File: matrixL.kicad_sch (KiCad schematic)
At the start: 66 parts, among them SW1 SW_Push, SW10 SW_Push, SW11 SW_Push, SW12 SW_Push, SW13 SW_Push, SW14 SW_Push, SW15 SW_Push, SW16 SW_Push, SW17 SW_Push, SW18 SW_Push, SW19 SW_Push, SW2 SW_Push, SW20 SW_Push, SW21 SW_Push, SW22 SW_Push, SW23 SW_Push, SW24 SW_Push, SW25 SW_Push, SW26 SW_Push, SW27 SW_Push, SW28 SW_Push, SW29 SW_Push, SW3 SW_Push, SW30 SW_Push, SW31 SW_Push, SW32 SW_Push, SW33 SW_Push, SW4 SW_Push, SW5 SW_Push, SW6 SW_Push, SW7 SW_Push, SW8 SW_Push, SW9 SW_Push

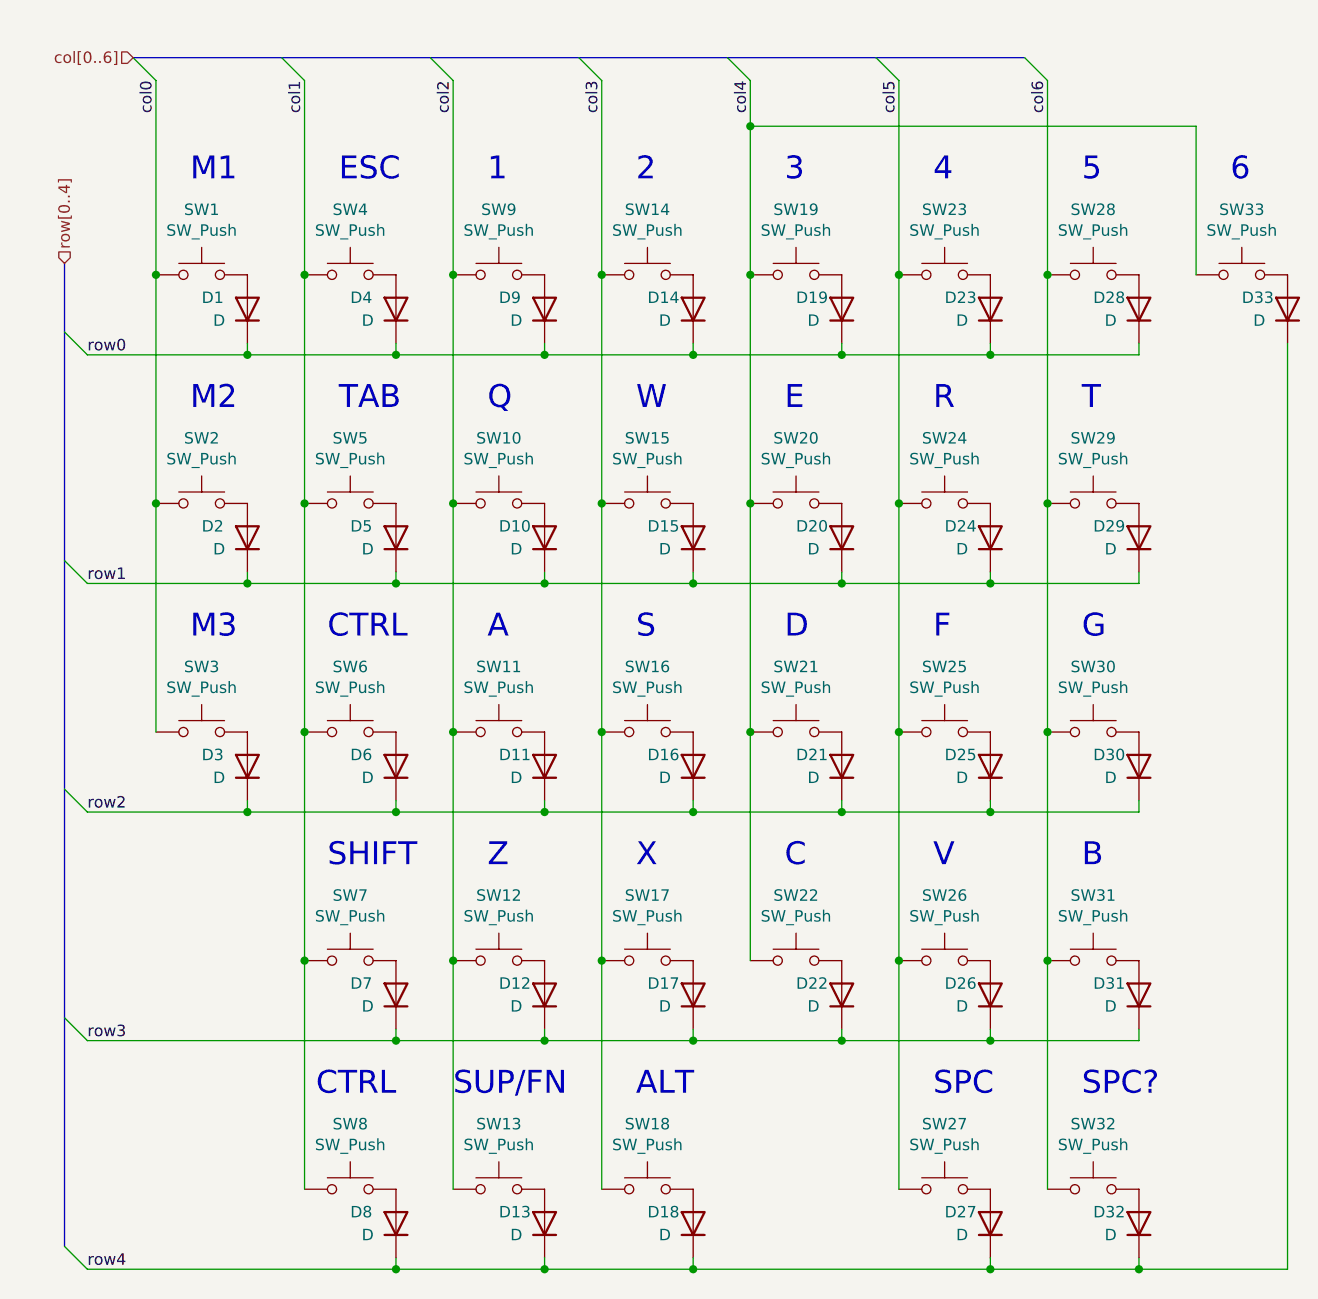
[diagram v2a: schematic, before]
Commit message: Add second micro back in, and added some footprints
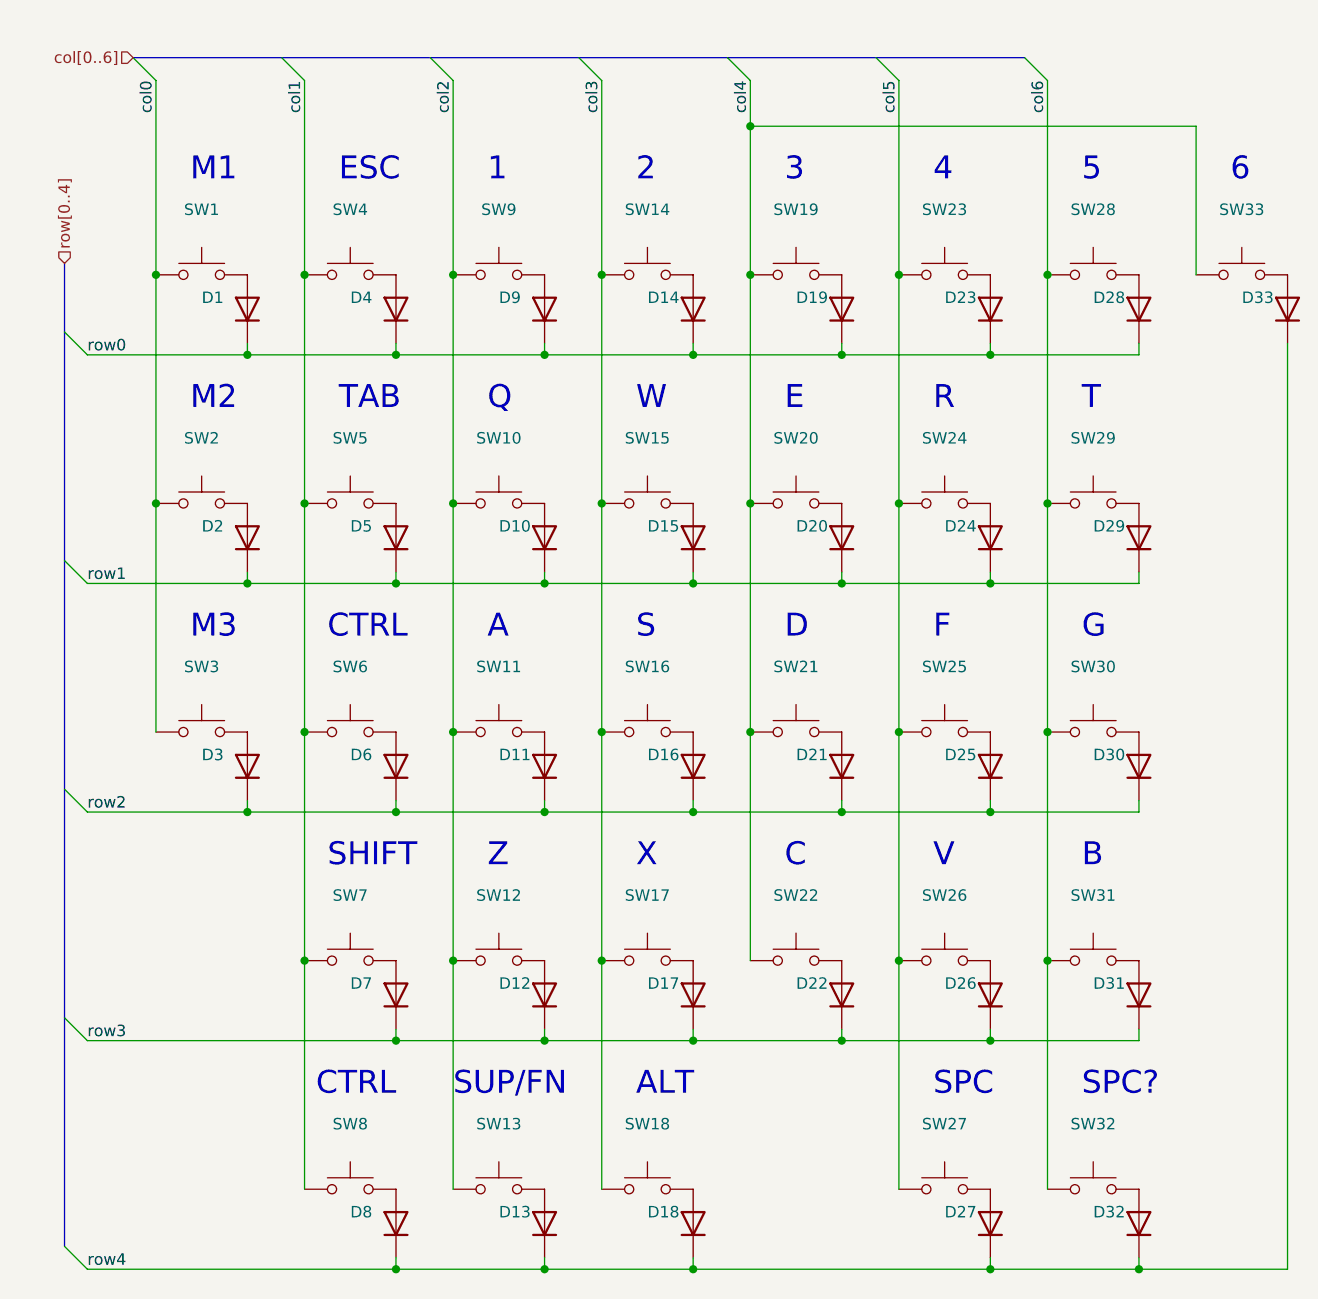
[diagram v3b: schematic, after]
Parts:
- D1, D10, D11, D12, D13, D14, D15, D16, D17, D18, D19, D2, D20, D21, D22, D23, D24, D25, D26, D27, D28, D29, D3, D30, D31, D32, D33, D4, D5, D6, D7, D8, D9: value D -> ~
- SW1, SW10, SW11, SW12, SW13, SW14, SW15, SW16, SW17, SW18, SW19, SW2, SW20, SW21, SW22, SW23, SW24, SW25, SW26, SW27, SW28, SW29, SW3, SW30, SW31, SW32, SW33, SW4, SW5, SW6, SW8, SW9: value SW_Push -> ~
- SW7: value SW_Push -> ~; footprint MX_Switch:SW_Cherry_MX_2.25u_PCB_Socket_ReversedStabilizers -> MX_Switch:SW_Cherry_MX_2.00u_PCB_Socket_ReversedStabilizers

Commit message: Fix left shift footprint, add stabilizer cutouts back in
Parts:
- SW7: footprint MX_Switch:SW_Cherry_MX_2.00u_PCB_Socket_ReversedStabilizers -> MX_Switch:SW_Cherry_MX_2.00u_PCB_Socket
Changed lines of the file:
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@@
     (property "Reference" "SW7" (id 0) (at 53.34 117.221 0))
     (property "Value" "~" (id 1) (at 53.34 119.5324 0))
-    (property "Footprint" "MX_Switch:SW_Cherry_MX_2.00u_PCB_Socket_ReversedStabilizers" (id 2) (at 53.34 119.38 0)
+    (property "Footprint" "MX_Switch:SW_Cherry_MX_2.00u_PCB_Socket" (id 2) (at 53.34 119.38 0)
       (effects (font (size 1.27 1.27)) hide)
     )
